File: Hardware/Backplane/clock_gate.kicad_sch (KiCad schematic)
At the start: 2 parts, among them U301 SN74LVC7001A

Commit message: Adjusts to review comments
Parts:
- C301: Digikey Part No (none) -> 399-C0603C104M4RACTUCT-ND
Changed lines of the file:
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@@
 			)
 		)
-		(property "Datasheet" ""
+		(property "Datasheet" "https://www.yageogroup.com/content/datasheet/asset/file/KEM_C1002_X7R_SMD"
 			(at 110.49 42.545 0)
 			(effects
@@
 			(at 110.49 42.545 0)
 			(effects
+				(font
+					(size 1.27 1.27)
+				)
+				(hide yes)
+			)
+		)
+		(property "Digikey Part No" "399-C0603C104M4RACTUCT-ND"
+			(at 110.49 42.545 0)
+			(effects

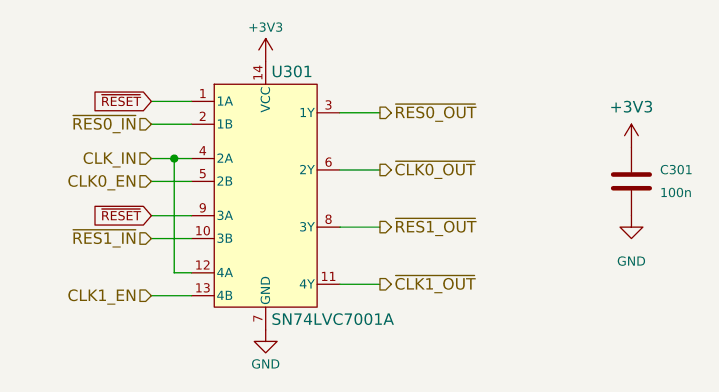
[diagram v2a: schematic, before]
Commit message: Starts refactoring Backplane to use NL17SZS11-D instead of 4-port AND
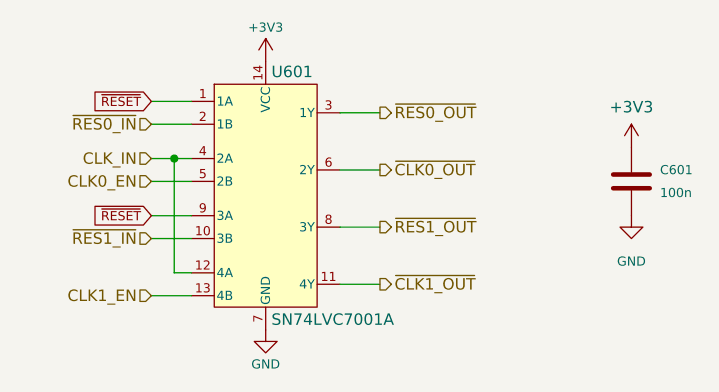
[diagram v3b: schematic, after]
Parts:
- renumbered C301 to C601, U301 to U601
